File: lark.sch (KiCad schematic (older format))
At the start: 39 parts, among them J1 SPI, J2 UART0, J3 I2C_0, SW1 SW_ENTR, SW2 SW_UP, SW3 SW_DOWN, SW4 SW_VARIO

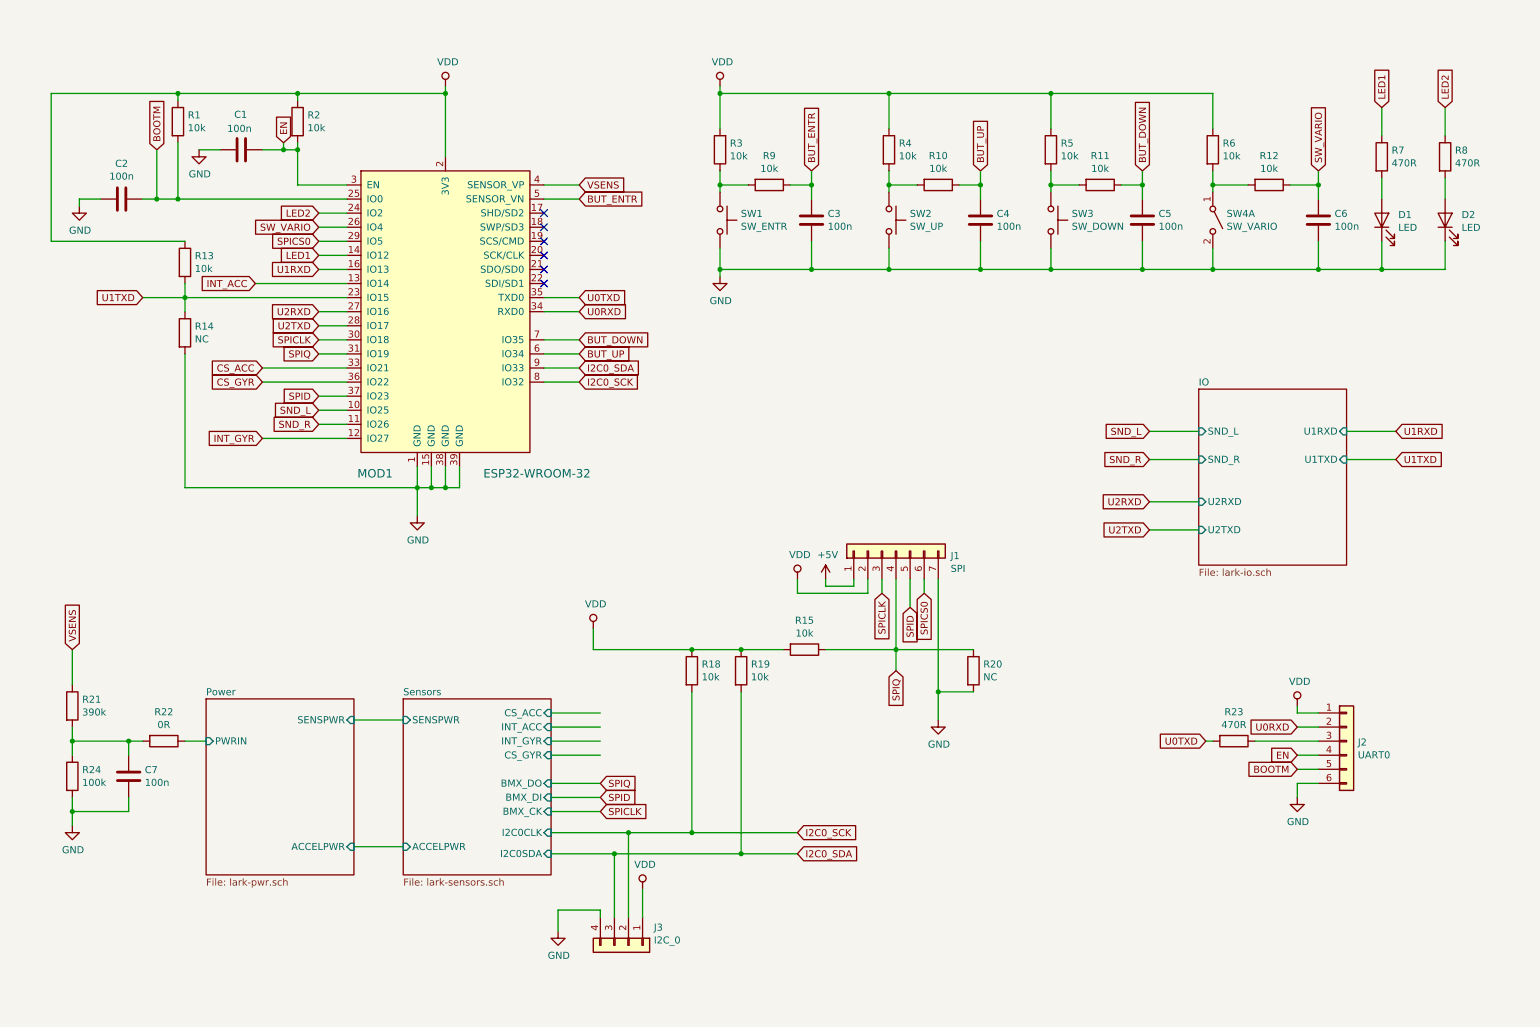
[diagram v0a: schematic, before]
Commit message: Use BMI088 instead of BMX055.
Symbol for BMI088 was created and placed in the schematic.

Still looking for a LGA-16 4.5x3.0 footprint. Do we really need to
create that ourselves?
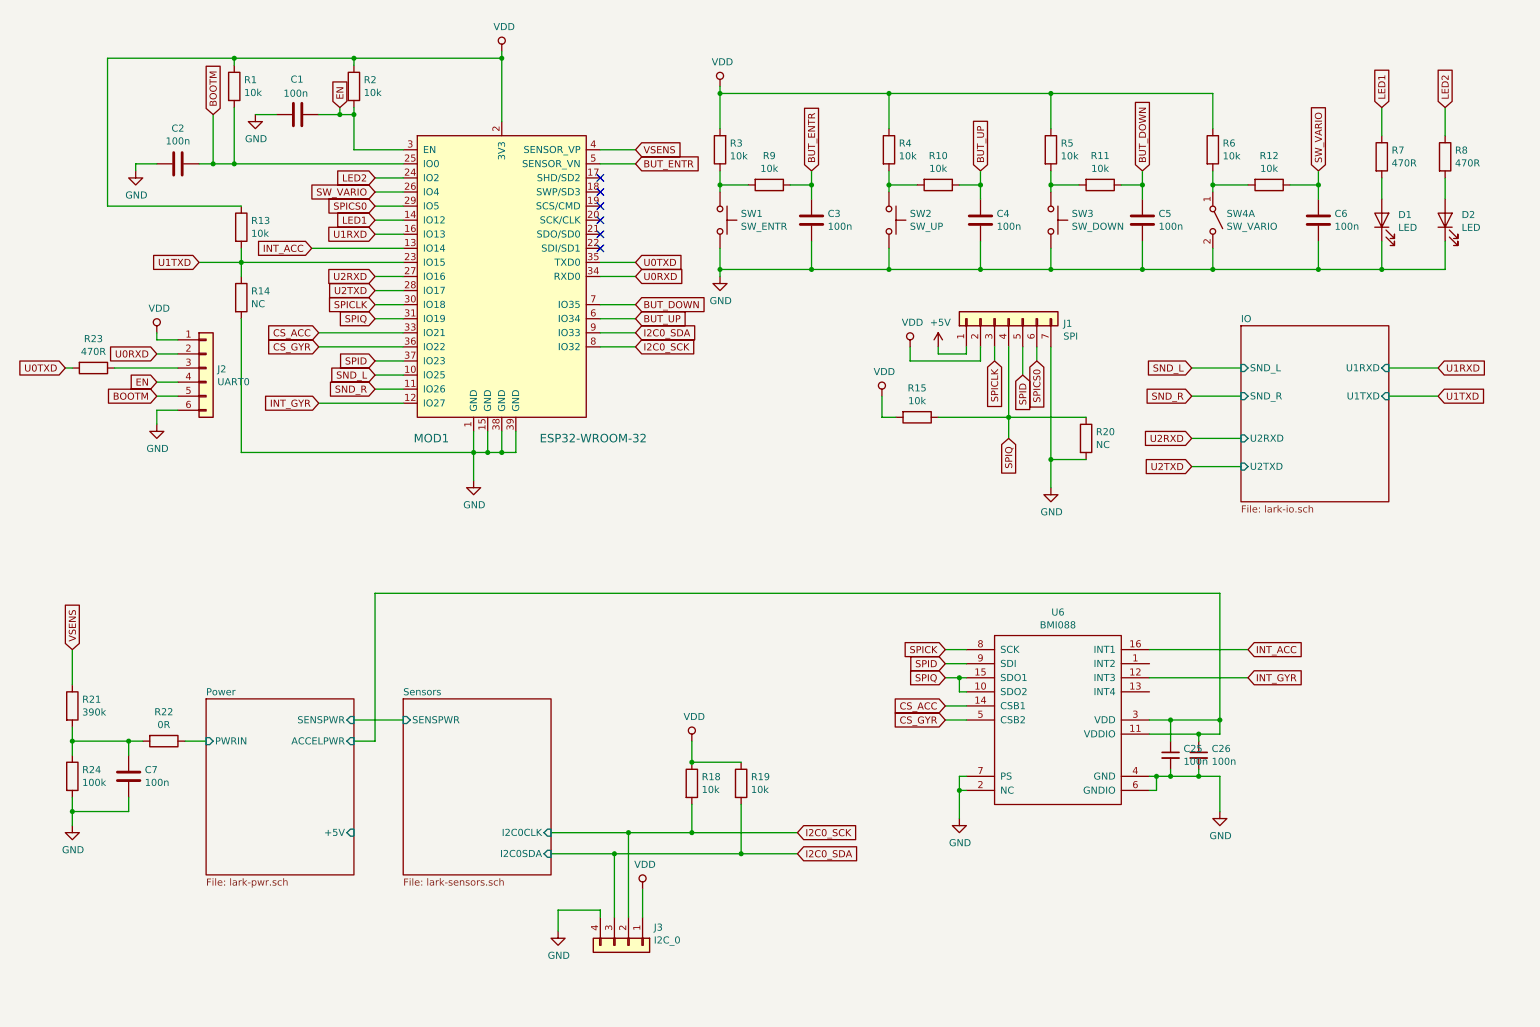
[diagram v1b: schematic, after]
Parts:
- added C25, C26: 100n, symbol Device:C_Small
- added U6: BMI088, symbol sensors:BMI088
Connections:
- net CS_ACC: now also U6.14 (CSB1)
- net CS_GYR: now also U6.5 (CSB2)
- net GND: now also C25.2, C26.2, U6.2 (NC), U6.4 (GND), U6.6 (GNDIO), U6.7 (PS)
- net INT_ACC: now also U6.16 (INT1)
- net INT_GYR: now also U6.12 (INT3)
- net Power/ACCELPWR: now also C25.1, C26.1, U6.11 (VDDIO), U6.3 (VDD)
- net SPID: now also U6.9 (SDI)
- net SPIQ: now also U6.10 (SDO2), U6.15 (SDO1)
- new net SPICK: U6.8 (SCK)
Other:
- moved on the sheet: C1, C2, J1, J2, MOD1, R1, R13, R14, R15, R18, R19, R2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

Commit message: Fitting layout into 57 mm instrument.
* board width is 51 mm at the moment
* split into two boards (sensor and main) which can be stacked with
  2.54 mm pinheaders.
* ESP32 was put to bottom with optional pcb antenna facing to front.
* added footprint for optional HCLAxxE on sensorboard
* added footprint for BMI088

* Is multiple GND pins for sensor board really a good idea (ground loops)?
* Does the +12V topology make sense (especially regarding the external
  IGC ports)?
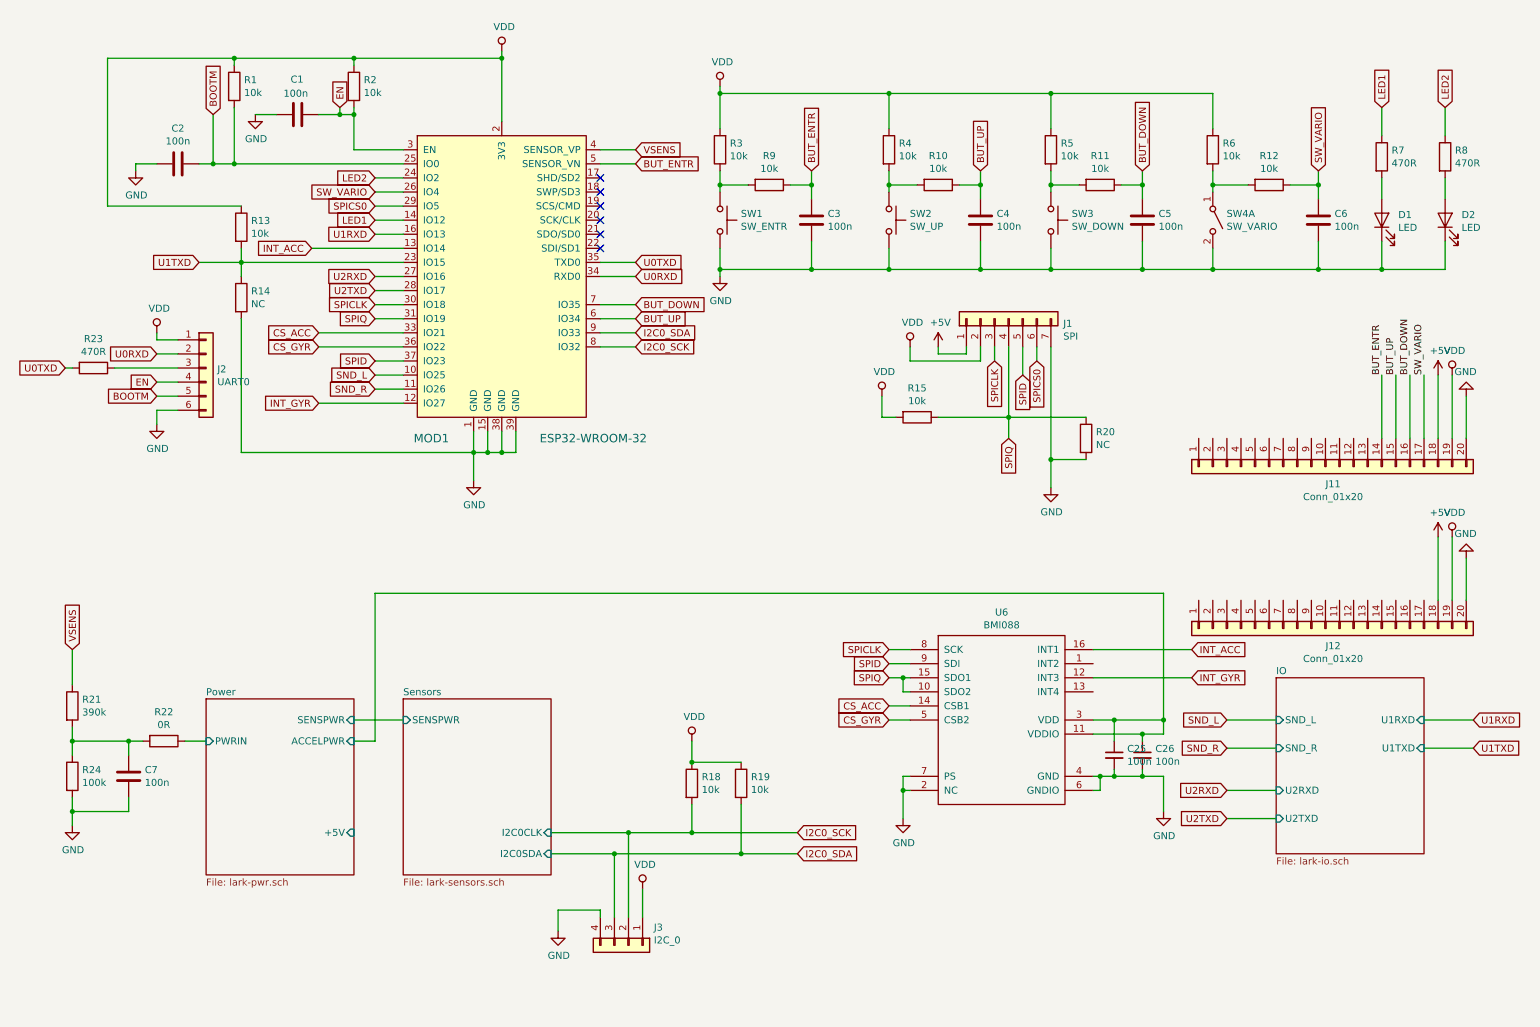
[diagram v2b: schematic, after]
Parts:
- added J11, J12: Conn_01x20, Connector_PinSocket_2.54mm:PinSocket_1x20_P2.54mm_Vertical, symbol Connector_Generic:Conn_01x20
- C25, C26: footprint (none) -> Capacitor_SMD:C_0805_2012Metric_Pad1.15x1.40mm_HandSolder
- U6: footprint (none) -> libs:LGA-16_handsolder
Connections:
- net SPICK is gone; now on net SPICLK: U6.8 (SCK)
- net +5V: now also J11.18 (Pin_18), J12.18 (Pin_18)
- net BUT_DOWN: now also J11.16 (Pin_16)
- net BUT_ENTR: now also J11.14 (Pin_14)
- net BUT_UP: now also J11.15 (Pin_15)
- net GND: now also J11.20 (Pin_20), J12.20 (Pin_20)
- net SW_VARIO: now also J11.17 (Pin_17)
- net VDD: now also J11.19 (Pin_19), J12.19 (Pin_19)
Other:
- moved on the sheet: C25, C26, U6

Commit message: Layout almost complete.
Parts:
- removed C26: 100n, Capacitor_SMD:C_0805_2012Metric_Pad1.15x1.40mm_HandSolder, symbol Device:C_Small
- removed C3, C4, C5, C6: 100n, Capacitor_SMD:C_0805_2012Metric_Pad1.15x1.40mm_HandSolder, symbol lark-rescue:C-Device
- removed J1: SPI, Connector_PinHeader_2.54mm:PinHeader_1x07_P2.54mm_Vertical, symbol lark-rescue:Conn_01x07-Connector_Generic
- removed J11: Conn_01x20, Connector_PinSocket_2.54mm:PinSocket_1x20_P2.54mm_Vertical, symbol Connector_Generic:Conn_01x20
- removed J2: UART0, Connector_PinHeader_2.54mm:PinHeader_1x06_P2.54mm_Vertical, symbol lark-rescue:Conn_01x06-Connector_Generic
- removed J3: I2C_0, Connector_PinHeader_2.54mm:PinHeader_1x04_P2.54mm_Vertical, symbol lark-rescue:Conn_01x04-Connector_Generic
- removed R10, R11, R12, R3, R4, R5, R6, R9: 10k, Resistor_SMD:R_0805_2012Metric_Pad1.15x1.40mm_HandSolder, symbol lark-rescue:R-Device
- removed SW1: SW_ENTR, Button_Switch_THT:SW_Tactile_SPST_Angled_PTS645Vx83-2LFS, symbol lark-rescue:SW_Push-Switch
- removed SW2: SW_UP, Button_Switch_THT:SW_Tactile_SPST_Angled_PTS645Vx83-2LFS, symbol lark-rescue:SW_Push-Switch
- removed SW3: SW_DOWN, Button_Switch_THT:SW_Tactile_SPST_Angled_PTS645Vx83-2LFS, symbol lark-rescue:SW_Push-Switch
- removed SW4: SW_VARIO, TerminalBlock_Phoenix:TerminalBlock_Phoenix_PT-1,5-2-3.5-H_1x02_P3.50mm_Horizontal, symbol lark-rescue:SW_DPST_x2-Switch
- added H1, H2, H3, H4: MountingHole, MountingHole:MountingHole_3.2mm_M3_DIN965, symbol Mechanical:MountingHole
- added J1: CONN1, Connector_PinHeader_2.54mm:PinHeader_1x15_P2.54mm_Vertical, symbol Connector_Generic:Conn_01x15
- added J3, J6: Conn_01x05-Connector_Generic, Connector_PinHeader_2.54mm:PinHeader_1x05_P2.54mm_Vertical, symbol lark-rescue:Conn_01x05-Connector_Generic
- J11: renamed from J12; value Conn_01x20 -> CONN1; footprint Connector_PinSocket_2.54mm:PinSocket_1x20_P2.54mm_Vertical -> Connector_PinHeader_2.54mm:PinHeader_1x15_P2.54mm_Vertical; symbol Connector_Generic:Conn_01x20 -> Connector_Generic:Conn_01x15
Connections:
- net +5V: now also J11.3 (Pin_3), J1.3 (Pin_3), J3.1 (Pin_1); no longer J11.18 (Pin_18)
- net BOOTM: now also J11.12 (Pin_12)
- net BUT_DOWN: now also J1.6 (Pin_6)
- net BUT_ENTR: now also J1.4 (Pin_4)
- net BUT_UP: now also J1.5 (Pin_5)
- net EN: now also J11.11 (Pin_11)
- net GND: now also J11.1 (Pin_1), J11.13 (Pin_13), J1.1 (Pin_1), J3.5 (Pin_5); no longer J11.20 (Pin_20)
- net I2C0_SCK: now also J3.4 (Pin_4)
- net I2C0_SDA: now also J3.3 (Pin_3)
- net LED1: now also J1.9 (Pin_9)
- net LED2: now also J1.8 (Pin_8)
- net SPICLK: now also J11.6 (Pin_6)
- net SPICS0: now also J11.7 (Pin_7)
- net SPID: now also J11.4 (Pin_4)
- net SPIQ: now also J11.5 (Pin_5)
- net SW_VARIO: now also J1.7 (Pin_7)
- net U0RXD: now also J11.9 (Pin_9)
- net VDD: now also J11.2 (Pin_2), J11.8 (Pin_8), J1.2 (Pin_2); no longer J11.19 (Pin_19)
- net at R23.1: now also J11.10 (Pin_10)
- no-connect marks 6 -> 12
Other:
- moved on the sheet: D1, D2, R15, R18, R19, R20, R23, R7, R8
